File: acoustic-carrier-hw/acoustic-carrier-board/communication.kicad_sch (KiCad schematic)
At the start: 55 parts, among them IC1 ECP5-BGA256, J3 8P8C_Shielded, U1 KSZ9031RN, Y1 25MHz

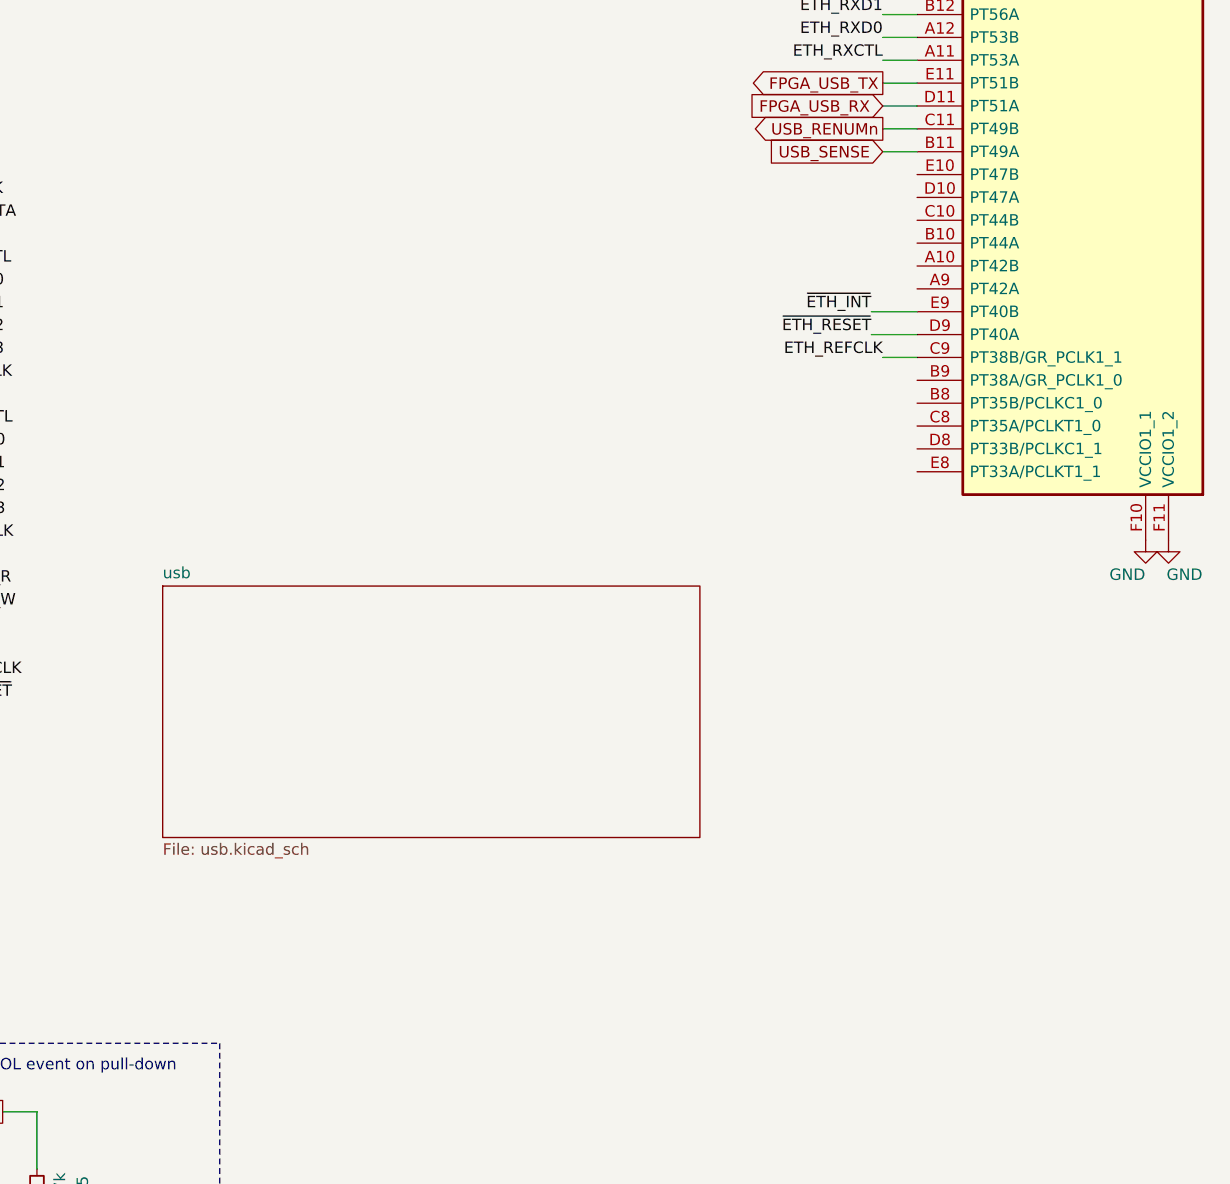
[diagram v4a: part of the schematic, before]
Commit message: [carrier] Added adc connections and PWM + poweer connectors
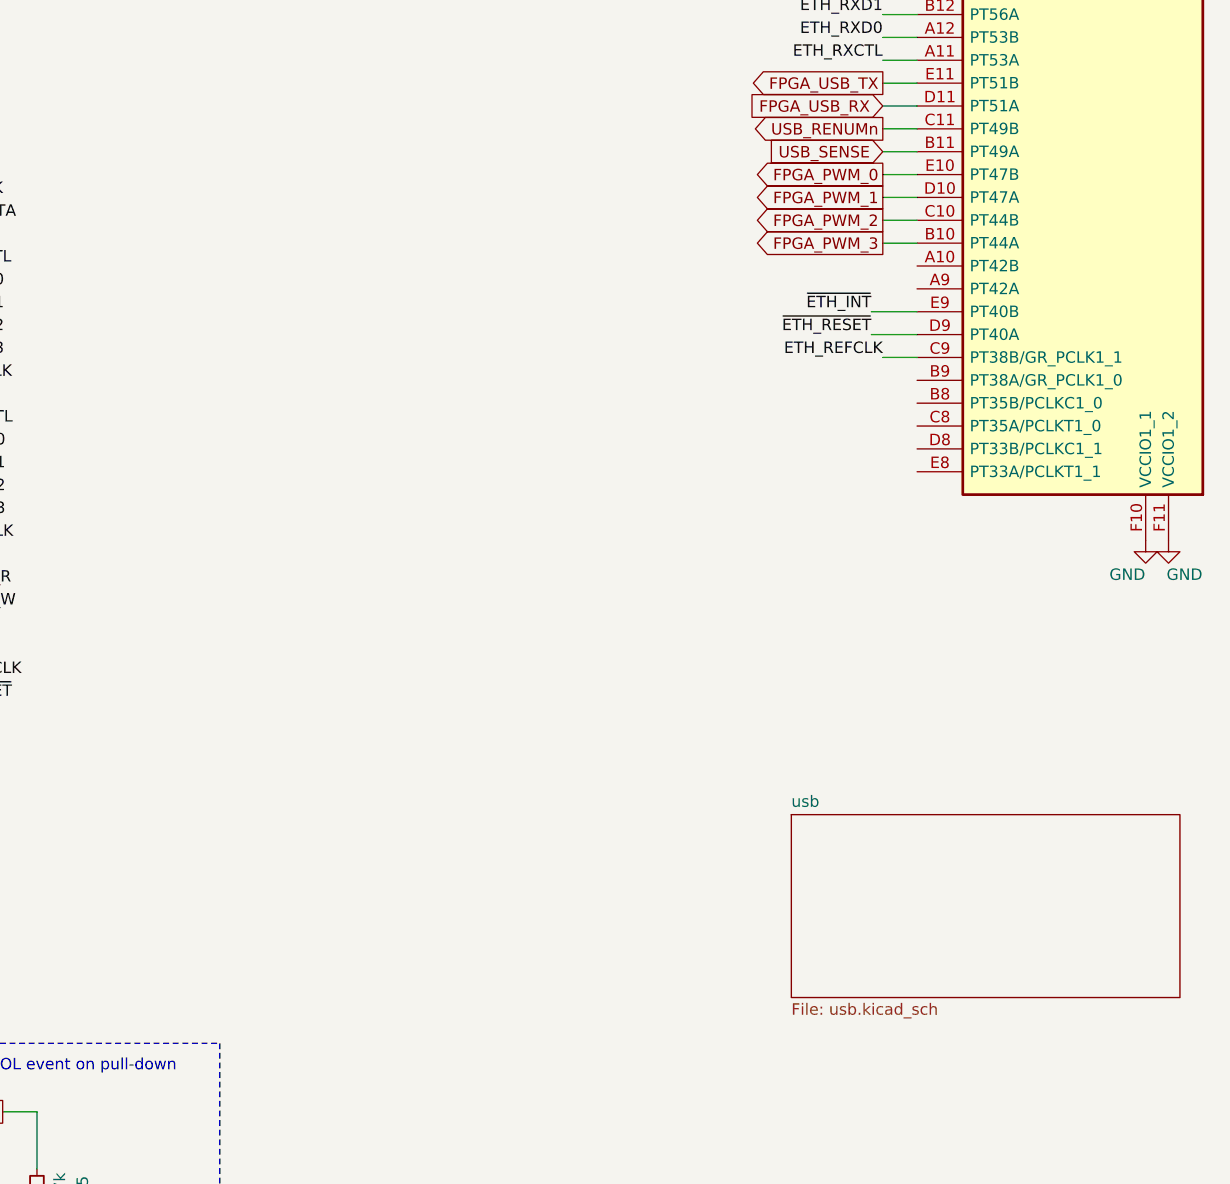
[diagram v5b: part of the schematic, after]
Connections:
- net FPGA_PWM_3: now reaches IC1.B10 (PT44A)
- net FPGA_PWM_2: now reaches IC1.C10 (PT44B)
- net FPGA_PWM_1: now reaches IC1.D10 (PT47A)
- net FPGA_PWM_0: now reaches IC1.E10 (PT47B)
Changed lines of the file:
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@@
 	(wire
 		(pts
+			(xy 245.11 67.31) (xy 248.92 67.31)
+		)
+		(stroke
+			(width 0)
+			(type default)
+		)
+	)
+	(wire
+		(pts
 			(xy 81.28 46.99) (xy 81.28 45.72)
 		)
@@
 		)
 	)
+	(wire
+		(pts
+			(xy 245.11 74.93) (xy 248.92 74.93)
+		)
+		(stroke
+			(width 0)
+			(type default)
+		)
+	)
 	(polyline
 		(pts
@@
 	(wire
 		(pts
+			(xy 245.11 69.85) (xy 248.92 69.85)
+		)
+		(stroke
+			(width 0)
+			(type default)
+		)
+	)
+	(wire
+		(pts
 			(xy 81.28 161.29) (xy 81.28 162.56)
 		)
@@
 	(wire
 		(pts
+			(xy 245.11 72.39) (xy 248.92 72.39)
+		)
+		(stroke
+			(width 0)
+			(type default)
+		)
+	)
+	(wire
+		(pts
 			(xy 248.92 41.91) (xy 245.11 41.91)
 		)
@@
 		)
 	)
+	(global_label "FPGA_PWM_1"
+		(shape output)
+		(at 245.11 69.85 180)
+		(fields_autoplaced yes)
+		(effects
+			(font
+				(size 1.27 1.27)
+			)
+			(justify right)
+		)
+		(property "Intersheetrefs" "${INTERSHEET_REFS}"
+			(at 230.0901 69.85 0)
+			(effects
+				(font
+					(size 1.27 1.27)
+				)
+				(justify right)
+				(hide yes)
+			)
+		)
+	)
 	(global_label "VETH_1V2"
 		(shape passive)
@@
 		)
 	)
+	(global_label "FPGA_PWM_0"
+		(shape output)
+		(at 245.11 67.31 180)
+		(fields_autoplaced yes)
+		(effects
+			(font
+				(size 1.27 1.27)
+			)
+			(justify right)
+		)
+		(property "Intersheetrefs" "${INTERSHEET_REFS}"
+			(at 230.0901 67.31 0)
+			(effects
+				(font
+					(size 1.27 1.27)
+				)
+				(justify right)
+				(hide yes)
+			)
+		)
+	)
 	(global_label "USB_SENSE"
 		(shape input)
@@
 		)
 	)
+	(global_label "FPGA_PWM_2"
+		(shape output)
+		(at 245.11 72.39 180)
+		(fields_autoplaced yes)
+		(effects
+			(font
+				(size 1.27 1.27)
+			)
+			(justify right)
+		)
+		(property "Intersheetrefs" "${INTERSHEET_REFS}"
+			(at 230.0901 72.39 0)
+			(effects
+				(font
+					(size 1.27 1.27)
+				)
+				(justify right)
+				(hide yes)
+			)
+		)
+	)
 	(global_label "VCORE_3V3"
 		(shape passive)
@@
 		)
 	)
+	(global_label "FPGA_PWM_3"
+		(shape output)
+		(at 245.11 74.93 180)
+		(fields_autoplaced yes)
+		(effects
+			(font
+				(size 1.27 1.27)
+			)
+			(justify right)
+		)
+		(property "Intersheetrefs" "${INTERSHEET_REFS}"
+			(at 230.0901 74.93 0)
+			(effects
+				(font
+					(size 1.27 1.27)
+				)
+				(justify right)
+				(hide yes)
+			)
+		)
+	)
 	(global_label "VETH_1V2"
 		(shape passive)
@@
 	)
 	(sheet
-		(at 165.1 113.03)
-		(size 59.69 27.94)
+		(at 234.95 138.43)
+		(size 43.18 20.32)
 		(exclude_from_sim no)
 		(in_bom yes)
@@
 		)
 		(property "Sheetname" "usb"
-			(at 165.1 112.3184 0)
+			(at 234.95 137.7184 0)
 			(effects
 				(font
@@
 		)
 		(property "Sheetfile" "usb.kicad_sch"
-			(at 165.1 141.5546 0)
+			(at 234.95 159.3346 0)
 			(effects
 				(font

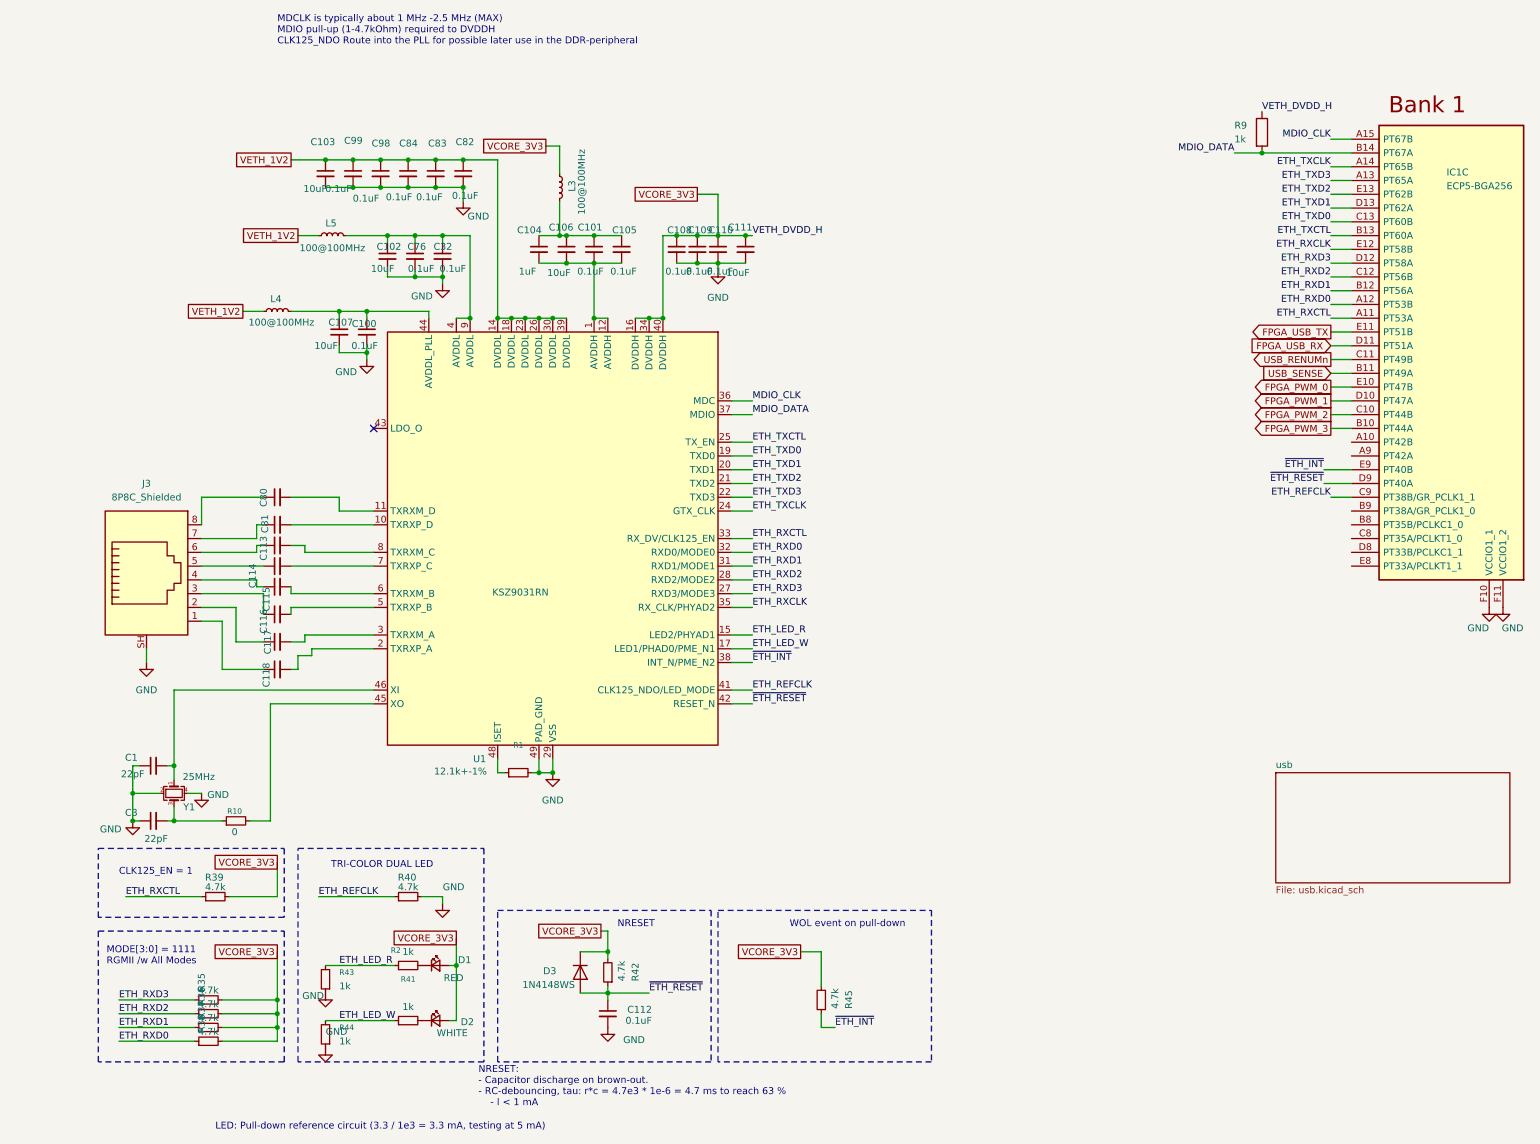
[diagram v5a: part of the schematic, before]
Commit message: [carrier] Reorganized carrier board schematic, added lcsc part numbers (next) check schematic before component placement
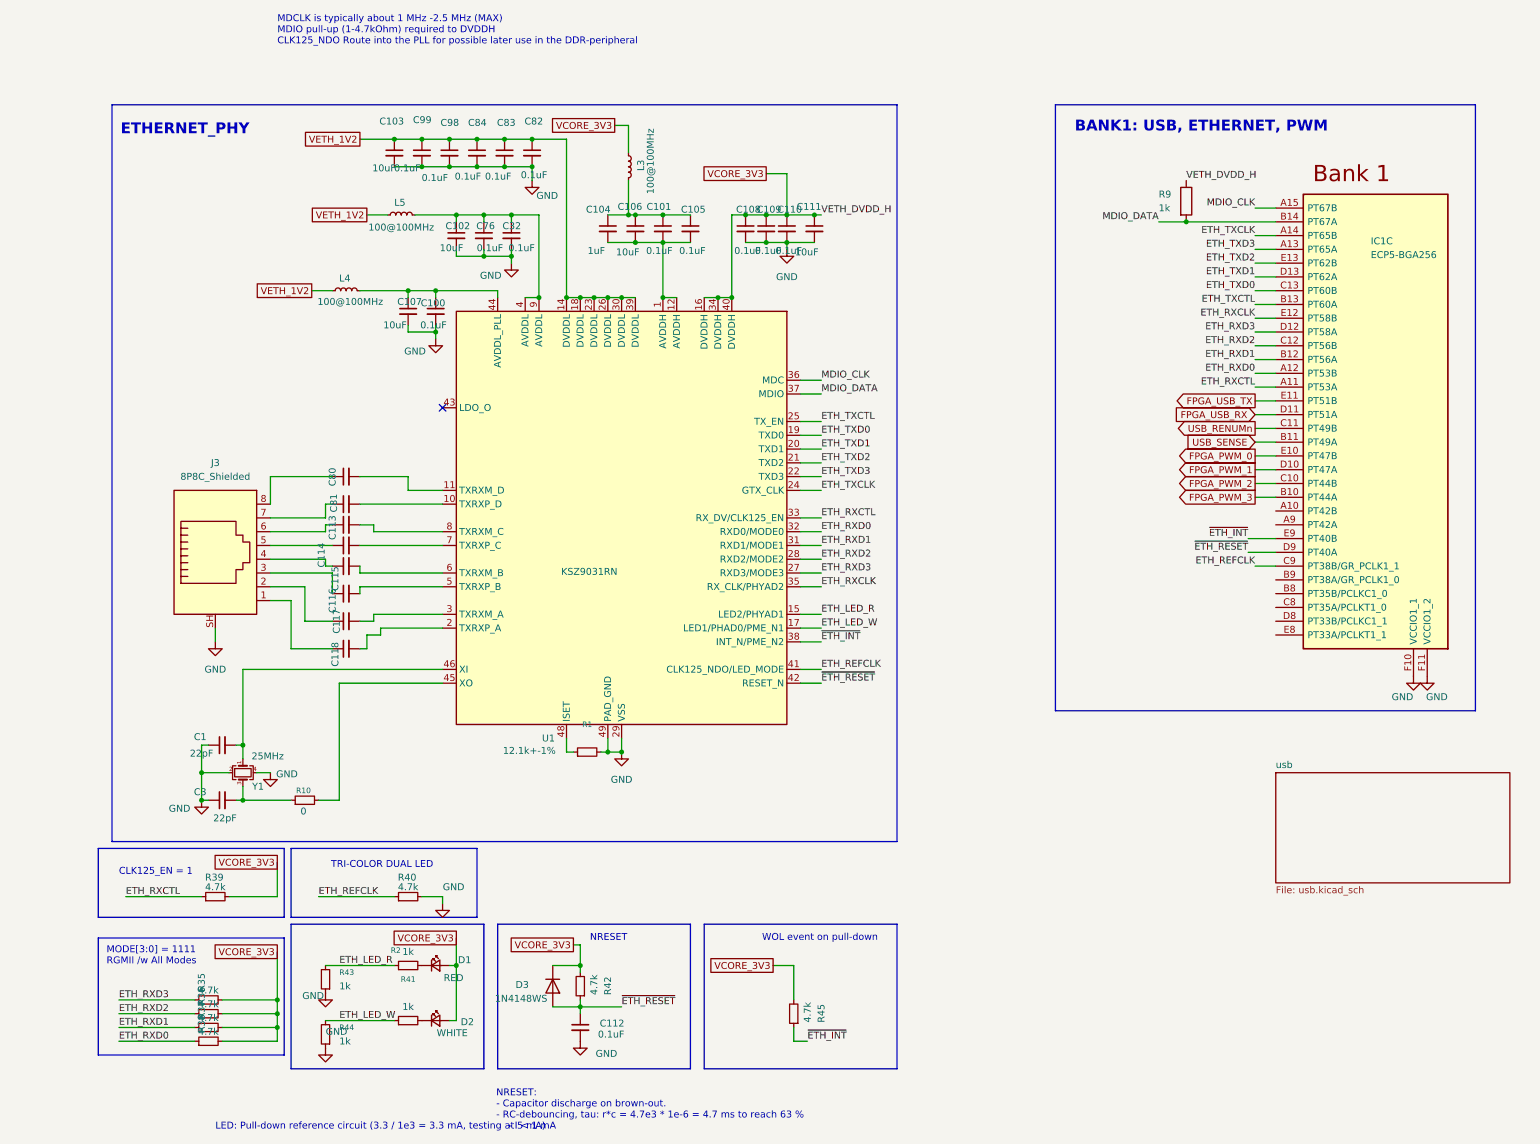
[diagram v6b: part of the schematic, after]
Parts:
- C100, C101, C105, C108, C109, C110, C112, C32, C76, C82, C83, C84, C98, C99: LCSC Part Number C307331 -> (none); LPN (none) -> C307331; MPN (none) -> CL05B104KB54PNC; Manufacturing Part Number CL05B104KB54PNC -> (none)
- C102, C103, C106, C107, C111: LCSC Part Number C19702 -> (none); LPN (none) -> C19702; MPN (none) -> CL10A106KP8NNNC; Manufacturing Part Number CL10A106KP8NNNC -> (none)
- C104: LCSC Part Number C28323 -> (none); LPN (none) -> C28323; MPN (none) -> CL21B105KBFNNNE; Manufacturing Part Number CL21B105KBFNNNE -> (none)
- C113, C114, C115, C116, C117, C118, C80, C81: LCSC Part Number C88136 -> (none); LPN (none) -> C88136; MPN (none) -> 0603B104J500NT; Manufacturing Part Number 0603B104J500NT -> (none)
- J3: LCSC Part Number C708652 -> (none); LPN (none) -> C708652; MPN (none) -> RC01937; Manufacturing Part Number RC01937 -> (none)
- R35, R36, R37, R38, R39, R40, R42, R45: LCSC Part Number C25900 -> (none); LPN (none) -> 0402WGF4701TCE; MPN (none) -> C25900; Manufacturing Part Number 0402WGF4701TCE -> (none)
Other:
- note added: "BANK1: USB, ETHERNET, PWM"
- note added: "ETHERNET_PHY"
- moved on the sheet: C1, C100, C101, C102, C103, C104, C105, C106, C107, C108, C109, C110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
